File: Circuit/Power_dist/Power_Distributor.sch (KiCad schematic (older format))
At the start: 1 part, among them J1 Thruster_Off_Switch

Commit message: edit sch and add pcix16
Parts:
- added CON1: Conn-PCIE-x16, zeabus:pcie-x16-edge, symbol Conn-PCIE-x16
- J1: symbol CONN_01X02 -> Conn_01x02
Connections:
- net labels added: +12V, +5V, D+, D-, GNDD, GNDREF, VBUS
- wire segments 35 -> 50

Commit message: change jp footprint
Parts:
- J1: footprint Socket_Strips:Socket_Strip_Straight_1x02_Pitch2.54mm -> Pin_Headers:Pin_Header_Straight_1x02_Pitch2.54mm
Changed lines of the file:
@@
 F 0 "J1" H 8050 1650 50  0000 C CNN
 F 1 "Thruster_Off_Switch" V 8150 1500 50  0000 C CNN
-F 2 "Socket_Strips:Socket_Strip_Straight_1x02_Pitch2.54mm" H 8050 1500 50  0001 C CNN
+F 2 "Pin_Headers:Pin_Header_Straight_1x02_Pitch2.54mm" H 8050 1500 50  0001 C CNN
 F 3 "" H 8050 1500 50  0001 C CNN
 	1    8050 1500

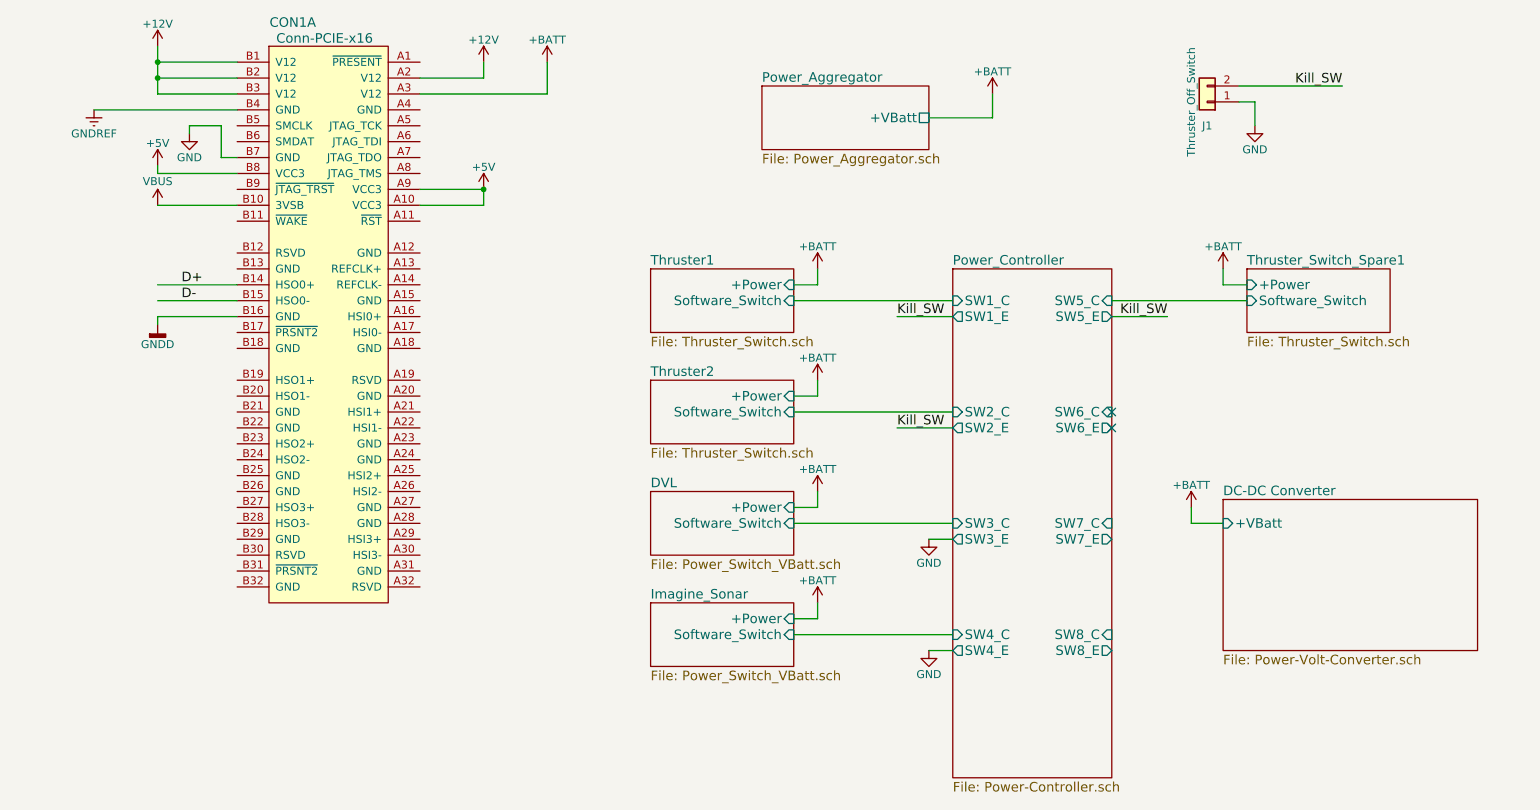
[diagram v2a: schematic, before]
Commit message: delete fuses at thrusters and oring + add power on jumper
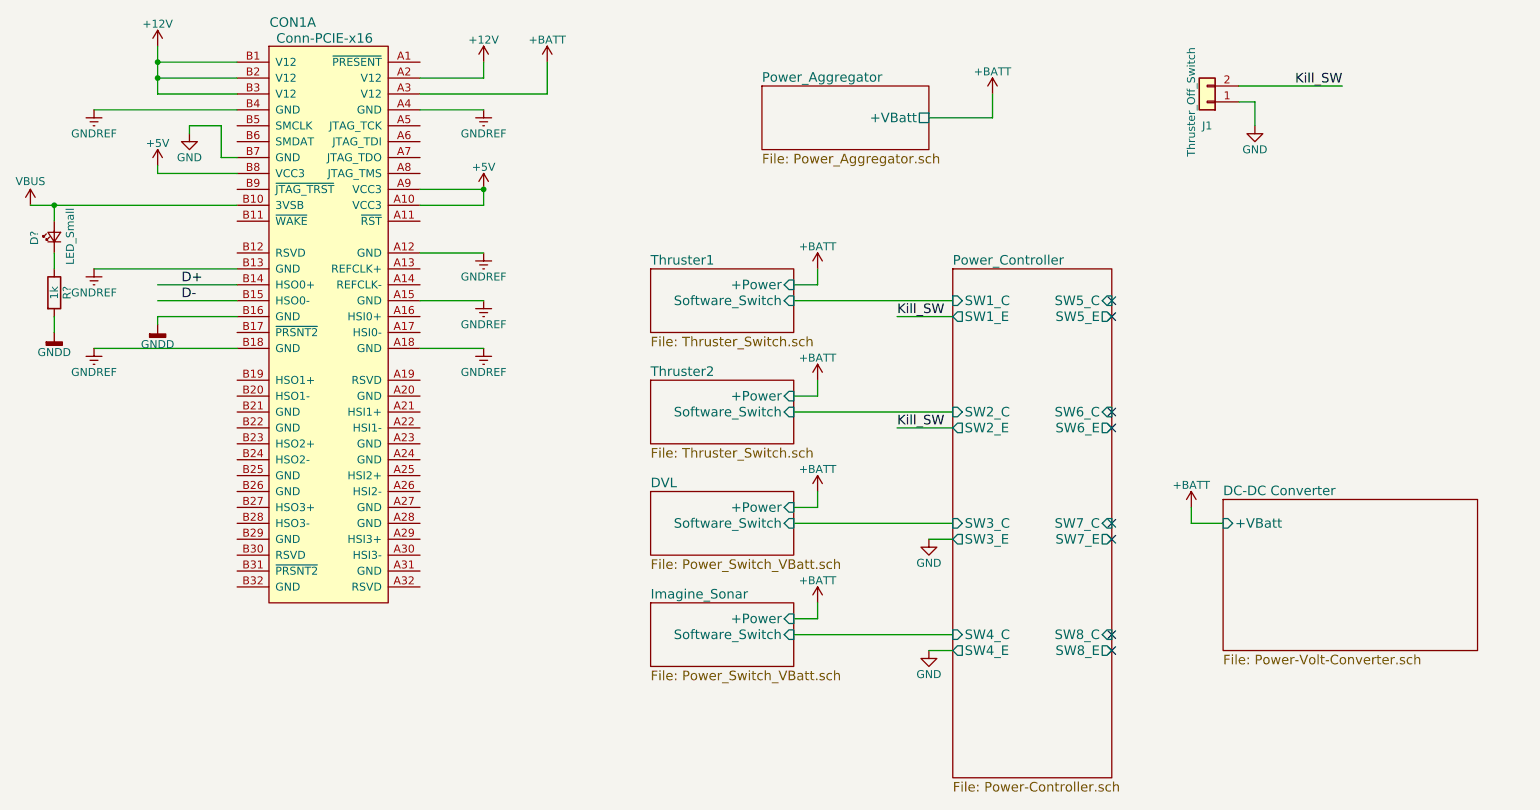
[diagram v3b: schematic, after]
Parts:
- added D?: LED_Small, symbol LED_Small
- added R?: 1k, symbol R
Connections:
- wire segments 50 -> 55
- no-connect marks 2 -> 8
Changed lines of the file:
@@
 $Descr A4 11693 8268
 encoding utf-8
-Sheet 1 9
+Sheet 1 8
 Title "Power Distributor"
 Date "2017-04-06"
@@
 F3 "Software_Switch" I R 5450 4850 60
 $EndSheet
-$Sheet
-S 8300 2550 900  400
-U 58E62AD5
-F0 "Thruster_Switch_Spare1" 60
-F1 "Thruster_Switch.sch" 60
-F2 "+Power" I L 8300 2650 60
-F3 "Software_Switch" I L 8300 2750 60
-$EndSheet
 $Comp
 L +BATT #PWR01
@@
 	1    0    0    -1
 $EndComp
-$Comp
-L +BATT #PWR07
-U 1 1 58EC0437
-P 8150 2550
-F 0 "#PWR07" H 8150 2400 50  0001 C CNN
-F 1 "+BATT" H 8150 2690 50  0000 C CNN
-F 2 "" H 8150 2550 50  0001 C CNN
-F 3 "" H 8150 2550 50  0001 C CNN
-	1    8150 2550
-	1    0    0    -1
-$EndComp
 $Sheet
 S 5250 1400 1050 400
@@
 Text Label 6100 3550 0    60   ~ 0
 Kill_SW
-Text Label 7800 2850 2    60   ~ 0
-Kill_SW
 NoConn ~ 7450 3450
 NoConn ~ 7450 3550
@@
 L VBUS #PWR011
 U 1 1 5A35B671
-P 1450 2150
-F 0 "#PWR011" H 1450 2000 50  0001 C CNN
-F 1 "VBUS" H 1450 2300 50  0000 C CNN
-F 2 "" H 1450 2150 50  0001 C CNN
-F 3 "" H 1450 2150 50  0001 C CNN
-	1    1450 2150
+P 650 2150
+F 0 "#PWR011" H 650 2000 50  0001 C CNN
+F 1 "VBUS" H 650 2300 50  0000 C CNN
+F 2 "" H 650 2150 50  0001 C CNN
+F 3 "" H 650 2150 50  0001 C CNN
+	1    650  2150
 	1    0    0    -1
 $EndComp
@@
 	5600 4750 5600 4650
 Wire Wire Line
-	8150 2550 8150 2650
-Wire Wire Line
-	8150 2650 8300 2650
-Wire Wire Line
 	6300 1600 6700 1600
 Wire Wire Line
@@
 	6450 2750 5450 2750
 Wire Wire Line
-	7450 2750 8300 2750
-Wire Wire Line
 	6100 2850 6450 2850
 Wire Wire Line
@@
 	6450 4950 6300 4950
 Wire Wire Line
-	7450 2850 7800 2850
-Wire Wire Line
 	1950 2750 1450 2750
 Wire Wire Line
 	1950 2650 1450 2650
 Wire Wire Line
-	1950 2150 1450 2150
+	650  2150 1950 2150
 Wire Wire Line
 	3500 2150 3100 2150
@@
 Wire Wire Line
 	1450 2850 1450 2900
+NoConn ~ 7450 2750
+NoConn ~ 7450 2850
+NoConn ~ 7450 4950
+NoConn ~ 7450 4850
+NoConn ~ 7450 4250
+NoConn ~ 7450 4150
+$Comp
+L GNDREF #PWR?
+U 1 1 5A395F6A
+P 3500 1550
+F 0 "#PWR?" H 3500 1300 50  0001 C CNN
+F 1 "GNDREF" H 3500 1400 50  0000 C CNN
+F 2 "" H 3500 1550 50  0001 C CNN
+F 3 "" H 3500 1550 50  0001 C CNN
+	1    3500 1550
+	1    0    0    -1
+$EndComp
+$Comp
+L GNDREF #PWR?
+U 1 1 5A396017
+P 3500 2450
+F 0 "#PWR?" H 3500 2200 50  0001 C CNN
+F 1 "GNDREF" H 3500 2300 50  0000 C CNN
+F 2 "" H 3500 2450 50  0001 C CNN
+F 3 "" H 3500 2450 50  0001 C CNN
+	1    3500 2450
+	1    0    0    -1
+$EndComp
+$Comp
+L GNDREF #PWR?
+U 1 1 5A3960CC
+P 3500 2750
+F 0 "#PWR?" H 3500 2500 50  0001 C CNN
+F 1 "GNDREF" H 3500 2600 50  0000 C CNN
+F 2 "" H 3500 2750 50  0001 C CNN
+F 3 "" H 3500 2750 50  0001 C CNN
+	1    3500 2750
+	1    0    0    -1
+$EndComp
+$Comp
+L GNDREF #PWR?
+U 1 1 5A396179
+P 3500 3050
+F 0 "#PWR?" H 3500 2800 50  0001 C CNN
+F 1 "GNDREF" H 3500 2900 50  0000 C CNN
+F 2 "" H 3500 3050 50  0001 C CNN
+F 3 "" H 3500 3050 50  0001 C CNN
+	1    3500 3050
+	1    0    0    -1
+$EndComp
+$Comp
+L GNDREF #PWR?
+U 1 1 5A396226
+P 1050 3050
+F 0 "#PWR?" H 1050 2800 50  0001 C CNN
+F 1 "GNDREF" H 1050 2900 50  0000 C CNN
+F 2 "" H 1050 3050 50  0001 C CNN
+F 3 "" H 1050 3050 50  0001 C CNN
+	1    1050 3050
+	1    0    0    -1
+$EndComp
+$Comp
+L GNDREF #PWR?
+U 1 1 5A3962D5
+P 1050 2550
+F 0 "#PWR?" H 1050 2300 50  0001 C CNN
+F 1 "GNDREF" H 1050 2400 50  0000 C CNN
+F 2 "" H 1050 2550 50  0001 C CNN
+F 3 "" H 1050 2550 50  0001 C CNN
+	1    1050 2550
+	1    0    0    -1
+$EndComp
+Wire Wire Line
+	1950 2550 1050 2550
+Wire Wire Line
+	1950 3050 1050 3050
+Wire Wire Line
+	3100 2450 3500 2450
+Wire Wire Line
+	3100 2750 3500 2750
+Wire Wire Line
+	3500 3050 3100 3050
+Wire Wire Line
+	3500 1550 3100 1550
+$Comp
+L LED_Small D?
+U 1 1 5A39F066
+P 800 2350
+F 0 "D?" H 750 2475 50  0000 L CNN
+F 1 "LED_Small" H 625 2250 50  0000 L CNN
+F 2 "" V 800 2350 50  0001 C CNN
+F 3 "" V 800 2350 50  0001 C CNN
+	1    800  2350
+	0    -1   -1   0
+$EndComp
+$Comp
+L R R?
+U 1 1 5A39F13D
+P 800 2700
+F 0 "R?" V 880 2700 50  0000 C CNN
+F 1 "1k" V 800 2700 50  0000 C CNN
+F 2 "" V 730 2700 50  0001 C CNN
+F 3 "" H 800 2700 50  0001 C CNN
+	1    800  2700
+	1    0    0    -1
+$EndComp
+$Comp
+L GNDD #PWR?
+U 1 1 5A39F866
+P 800 2950
+F 0 "#PWR?" H 800 2700 50  0001 C CNN
+F 1 "GNDD" H 800 2825 50  0000 C CNN
+F 2 "" H 800 2950 50  0001 C CNN
+F 3 "" H 800 2950 50  0001 C CNN
+	1    800  2950
+	1    0    0    -1
+$EndComp
+Wire Wire Line
+	800  2250 800  2150
+Connection ~ 800  2150
+Wire Wire Line
+	800  2450 800  2550
+Wire Wire Line
+	800  2850 800  2950
 $EndSCHEMATC

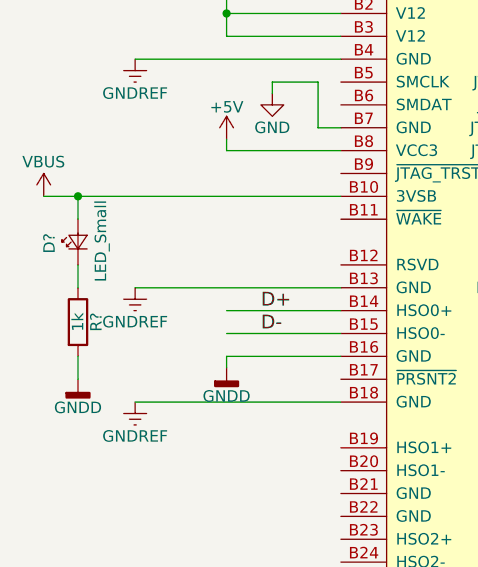
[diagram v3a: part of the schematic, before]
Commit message: component alignment on pcb
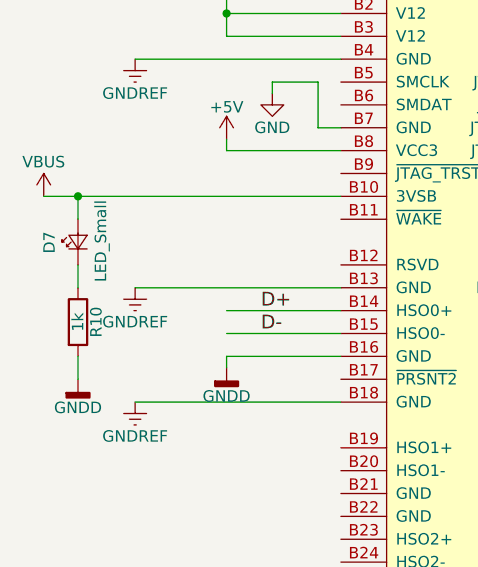
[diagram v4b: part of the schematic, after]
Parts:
- D7: renamed from D?; footprint (none) -> LEDs:LED_0603_HandSoldering
- R10: renamed from R?; footprint (none) -> Resistors_SMD:R_0603_HandSoldering
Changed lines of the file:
@@
 $EndSheet
 $Comp
-L +BATT #PWR08
+L +BATT #PWR07
 U 1 1 58E67F6C
 P 7950 4050
-F 0 "#PWR08" H 7950 3900 50  0001 C CNN
+F 0 "#PWR07" H 7950 3900 50  0001 C CNN
 F 1 "+BATT" H 7950 4190 50  0000 C CNN
 F 2 "" H 7950 4050 50  0001 C CNN
@@
 $EndComp
 $Comp
-L GND #PWR09
+L GND #PWR08
 U 1 1 58E66A79
 P 6300 4250
-F 0 "#PWR09" H 6300 4000 50  0001 C CNN
+F 0 "#PWR08" H 6300 4000 50  0001 C CNN
 F 1 "GND" H 6300 4100 50  0000 C CNN
 F 2 "" H 6300 4250 50  0001 C CNN
@@
 $EndComp
 $Comp
-L GND #PWR010
+L GND #PWR09
 U 1 1 58E66B6B
 P 6300 4950
-F 0 "#PWR010" H 6300 4700 50  0001 C CNN
+F 0 "#PWR09" H 6300 4700 50  0001 C CNN
 F 1 "GND" H 6300 4800 50  0000 C CNN
 F 2 "" H 6300 4950 50  0001 C CNN
@@
 D+
 $Comp
-L VBUS #PWR011
+L VBUS #PWR010
 U 1 1 5A35B671
 P 650 2150
-F 0 "#PWR011" H 650 2000 50  0001 C CNN
+F 0 "#PWR010" H 650 2000 50  0001 C CNN
 F 1 "VBUS" H 650 2300 50  0000 C CNN
 F 2 "" H 650 2150 50  0001 C CNN
@@
 $EndComp
 $Comp
-L +5V #PWR012
+L +5V #PWR011
 U 1 1 5A35C4C9
 P 3500 2050
-F 0 "#PWR012" H 3500 1900 50  0001 C CNN
+F 0 "#PWR011" H 3500 1900 50  0001 C CNN
 F 1 "+5V" H 3500 2190 50  0000 C CNN
 F 2 "" H 3500 2050 50  0001 C CNN
@@
 $EndComp
 $Comp
-L +5V #PWR013
+L +5V #PWR012
 U 1 1 5A35C7CC
 P 1450 1900
-F 0 "#PWR013" H 1450 1750 50  0001 C CNN
+F 0 "#PWR012" H 1450 1750 50  0001 C CNN
 F 1 "+5V" H 1450 2040 50  0000 C CNN
 F 2 "" H 1450 1900 50  0001 C CNN
@@
 Connection ~ 1450 1350
 $Comp
-L +12V #PWR014
+L +12V #PWR013
 U 1 1 5A360A30
 P 1450 1150
-F 0 "#PWR014" H 1450 1000 50  0001 C CNN
+F 0 "#PWR013" H 1450 1000 50  0001 C CNN
 F 1 "+12V" H 1450 1290 50  0000 C CNN
 F 2 "" H 1450 1150 50  0001 C CNN
@@
 $EndComp
 $Comp
-L +12V #PWR015
+L +12V #PWR014
 U 1 1 5A360B0A
 P 3500 1250
-F 0 "#PWR015" H 3500 1100 50  0001 C CNN
+F 0 "#PWR014" H 3500 1100 50  0001 C CNN
 F 1 "+12V" H 3500 1390 50  0000 C CNN
 F 2 "" H 3500 1250 50  0001 C CNN
@@
 	1850 1850 1950 1850
 $Comp
-L GNDD #PWR016
+L GNDD #PWR015
 U 1 1 5A363DC0
 P 1450 2900
-F 0 "#PWR016" H 1450 2650 50  0001 C CNN
+F 0 "#PWR015" H 1450 2650 50  0001 C CNN
 F 1 "GNDD" H 1450 2775 50  0000 C CNN
 F 2 "" H 1450 2900 50  0001 C CNN
@@
 $EndComp
 $Comp
-L GNDREF #PWR017
+L GNDREF #PWR016
 U 1 1 5A375B12
 P 1050 1550
-F 0 "#PWR017" H 1050 1300 50  0001 C CNN
+F 0 "#PWR016" H 1050 1300 50  0001 C CNN
 F 1 "GNDREF" H 1050 1400 50  0000 C CNN
 F 2 "" H 1050 1550 50  0001 C CNN
@@
 	3900 1450 3900 1250
 $Comp
-L +BATT #PWR018
+L +BATT #PWR017
 U 1 1 5A3576A9
 P 3900 1250
-F 0 "#PWR018" H 3900 1100 50  0001 C CNN
+F 0 "#PWR017" H 3900 1100 50  0001 C CNN
 F 1 "+BATT" H 3900 1390 50  0000 C CNN
 F 2 "" H 3900 1250 50  0001 C CNN
@@
 	1650 1650 1650 1700
 $Comp
-L GND #PWR019
+L GND #PWR018
 U 1 1 5A35E6F7
 P 1650 1700
-F 0 "#PWR019" H 1650 1450 50  0001 C CNN
+F 0 "#PWR018" H 1650 1450 50  0001 C CNN
 F 1 "GND" H 1650 1550 50  0000 C CNN
 F 2 "" H 1650 1700 50  0001 C CNN
@@
 NoConn ~ 7450 4150
 $Comp
-L GNDREF #PWR?
+L GNDREF #PWR019
 U 1 1 5A395F6A
 P 3500 1550
-F 0 "#PWR?" H 3500 1300 50  0001 C CNN
+F 0 "#PWR019" H 3500 1300 50  0001 C CNN
 F 1 "GNDREF" H 3500 1400 50  0000 C CNN
 F 2 "" H 3500 1550 50  0001 C CNN
@@
 $EndComp
 $Comp
-L GNDREF #PWR?
+L GNDREF #PWR020
 U 1 1 5A396017
 P 3500 2450
-F 0 "#PWR?" H 3500 2200 50  0001 C CNN
+F 0 "#PWR020" H 3500 2200 50  0001 C CNN
 F 1 "GNDREF" H 3500 2300 50  0000 C CNN
 F 2 "" H 3500 2450 50  0001 C CNN
@@
 $EndComp
 $Comp
-L GNDREF #PWR?
+L GNDREF #PWR021
 U 1 1 5A3960CC
 P 3500 2750
-F 0 "#PWR?" H 3500 2500 50  0001 C CNN
+F 0 "#PWR021" H 3500 2500 50  0001 C CNN
 F 1 "GNDREF" H 3500 2600 50  0000 C CNN
 F 2 "" H 3500 2750 50  0001 C CNN
@@
 $EndComp
 $Comp
-L GNDREF #PWR?
+L GNDREF #PWR022
 U 1 1 5A396179
 P 3500 3050
-F 0 "#PWR?" H 3500 2800 50  0001 C CNN
+F 0 "#PWR022" H 3500 2800 50  0001 C CNN
 F 1 "GNDREF" H 3500 2900 50  0000 C CNN
 F 2 "" H 3500 3050 50  0001 C CNN
@@
 $EndComp
 $Comp
-L GNDREF #PWR?
+L GNDREF #PWR023
 U 1 1 5A396226
 P 1050 3050
-F 0 "#PWR?" H 1050 2800 50  0001 C CNN
+F 0 "#PWR023" H 1050 2800 50  0001 C CNN
 F 1 "GNDREF" H 1050 2900 50  0000 C CNN
 F 2 "" H 1050 3050 50  0001 C CNN
@@
 $EndComp
 $Comp
-L GNDREF #PWR?
+L GNDREF #PWR024
 U 1 1 5A3962D5
 P 1050 2550
-F 0 "#PWR?" H 1050 2300 50  0001 C CNN
+F 0 "#PWR024" H 1050 2300 50  0001 C CNN
 F 1 "GNDREF" H 1050 2400 50  0000 C CNN
 F 2 "" H 1050 2550 50  0001 C CNN
@@
 	3500 1550 3100 1550
 $Comp
-L LED_Small D?
+L LED_Small D7
 U 1 1 5A39F066
 P 800 2350
-F 0 "D?" H 750 2475 50  0000 L CNN
+F 0 "D7" H 750 2475 50  0000 L CNN
 F 1 "LED_Small" H 625 2250 50  0000 L CNN
-F 2 "" V 800 2350 50  0001 C CNN
+F 2 "LEDs:LED_0603_HandSoldering" V 800 2350 50  0001 C CNN
 F 3 "" V 800 2350 50  0001 C CNN
 	1    800  2350
@@
 $EndComp
 $Comp
-L R R?
+L R R10
 U 1 1 5A39F13D
 P 800 2700
-F 0 "R?" V 880 2700 50  0000 C CNN
+F 0 "R10" V 880 2700 50  0000 C CNN
 F 1 "1k" V 800 2700 50  0000 C CNN
-F 2 "" V 730 2700 50  0001 C CNN
+F 2 "Resistors_SMD:R_0603_HandSoldering" V 730 2700 50  0001 C CNN
 F 3 "" H 800 2700 50  0001 C CNN
 	1    800  2700
@@
 $EndComp
 $Comp
-L GNDD #PWR?
+L GNDD #PWR025
 U 1 1 5A39F866
 P 800 2950
-F 0 "#PWR?" H 800 2700 50  0001 C CNN
+F 0 "#PWR025" H 800 2700 50  0001 C CNN
 F 1 "GNDD" H 800 2825 50  0000 C CNN
 F 2 "" H 800 2950 50  0001 C CNN

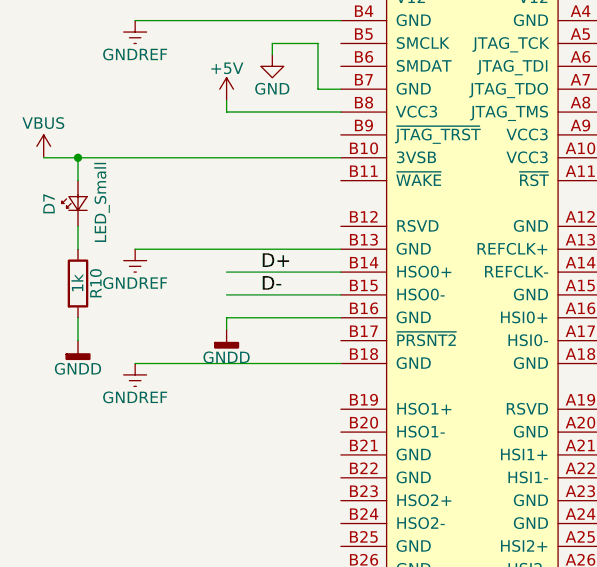
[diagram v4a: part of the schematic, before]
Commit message: fix USB_B Conn too far from edge
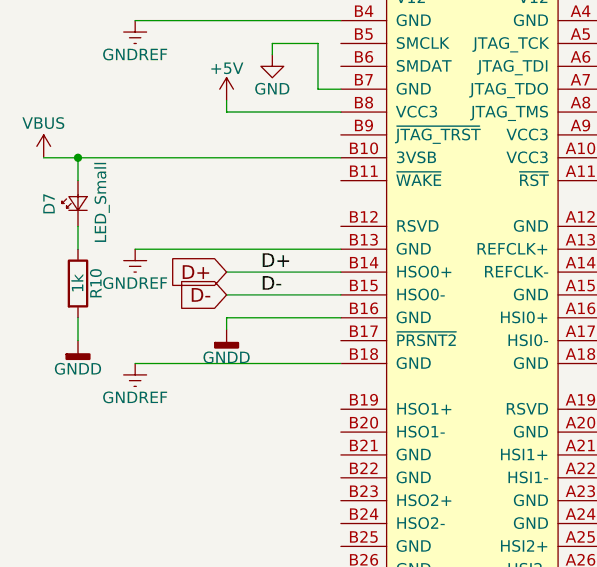
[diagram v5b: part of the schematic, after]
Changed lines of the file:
@@
 Wire Wire Line
 	800  2850 800  2950
+Text GLabel 1450 2650 0    60   Input ~ 0
+D+
+Text GLabel 1450 2750 0    60   Input ~ 0
+D-
 $EndSCHEMATC
